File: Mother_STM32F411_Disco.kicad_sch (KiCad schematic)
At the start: 15 parts

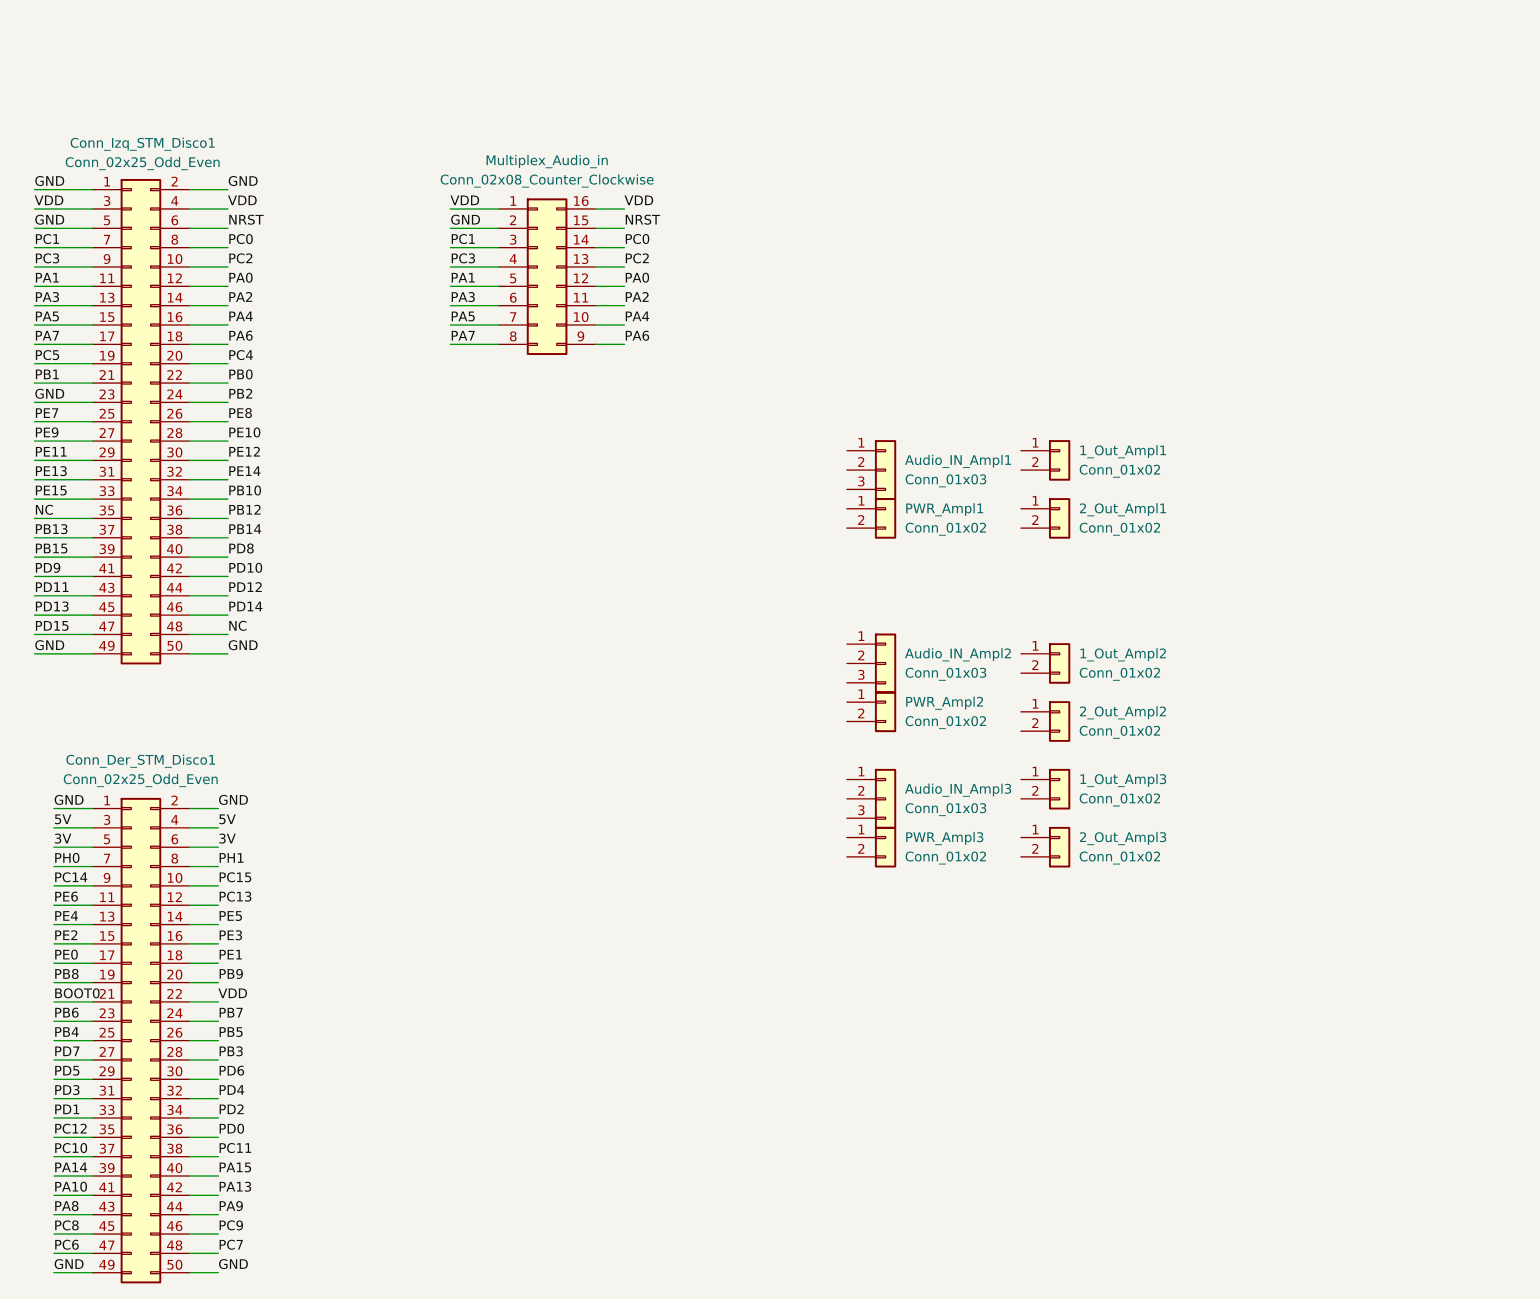
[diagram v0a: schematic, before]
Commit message: add modules in schematic
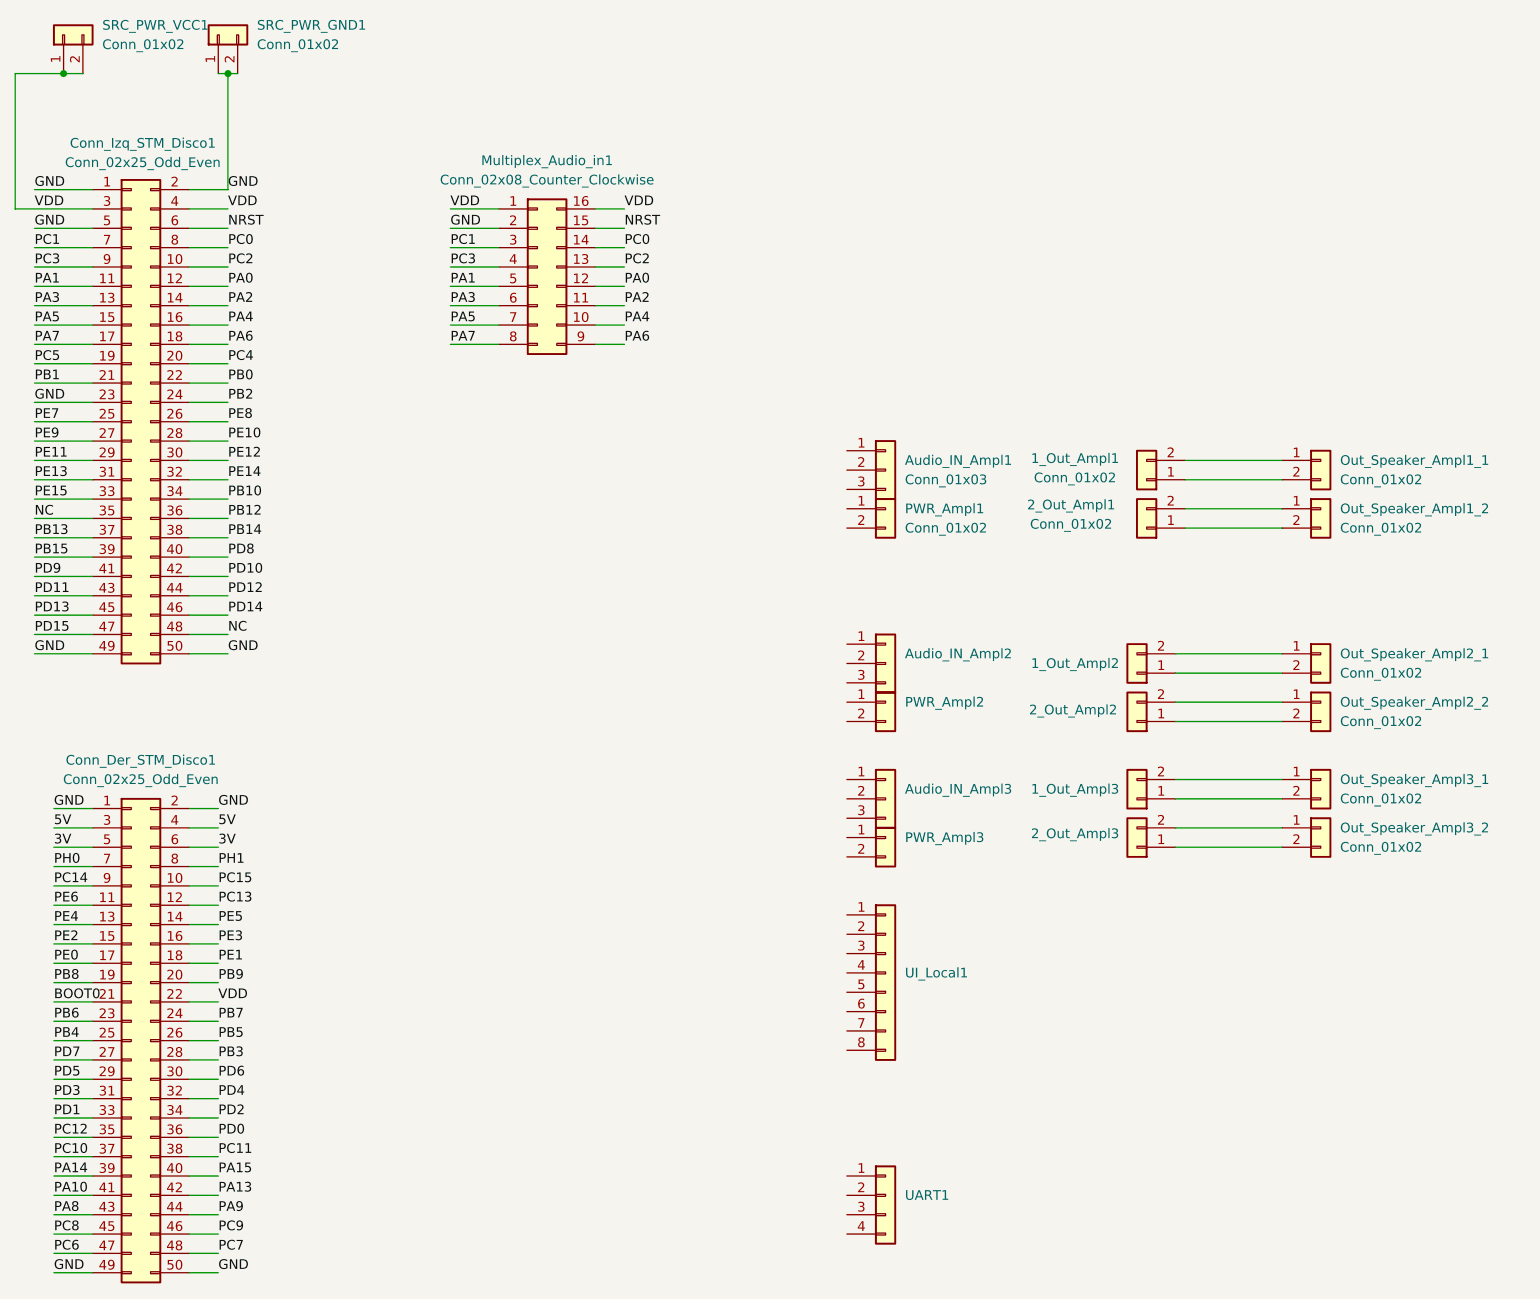
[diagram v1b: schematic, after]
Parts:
- added Out_Speaker_Ampl1_1, Out_Speaker_Ampl1_2, Out_Speaker_Ampl2_1, Out_Speaker_Ampl2_2, Out_Speaker_Ampl3_1, Out_Speaker_Ampl3_2: Conn_01x02, symbol Connector_Generic:Conn_01x02
- added SRC_PWR_GND1, SRC_PWR_VCC1: Conn_01x02, Connector_PinSocket_2.54mm:PinSocket_1x02_P2.54mm_Vertical, symbol Connector_Generic:Conn_01x02
- added UART1: Conn_01x04, symbol Connector_Generic:Conn_01x04
- added UI_Local1: Conn_01x08, symbol Connector_Generic:Conn_01x08
- renumbered Multiplex_Audio_in to Multiplex_Audio_in1
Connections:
- net GND: now also SRC_PWR_GND1.1 (Pin_1), SRC_PWR_GND1.2 (Pin_2)
- net VDD: now also SRC_PWR_VCC1.1 (Pin_1), SRC_PWR_VCC1.2 (Pin_2)
- net at 2_Out_Ampl2.1 (Pin_1): now also Out_Speaker_Ampl2_2.2 (Pin_2)
- net at 2_Out_Ampl2.2 (Pin_2): now also Out_Speaker_Ampl2_2.1 (Pin_1)
- net at 1_Out_Ampl2.1 (Pin_1): now also Out_Speaker_Ampl2_1.2 (Pin_2)
- net at 1_Out_Ampl2.2 (Pin_2): now also Out_Speaker_Ampl2_1.1 (Pin_1)
- net at 1_Out_Ampl1.1 (Pin_1): now also Out_Speaker_Ampl1_1.2 (Pin_2)
- net at 1_Out_Ampl1.2 (Pin_2): now also Out_Speaker_Ampl1_1.1 (Pin_1)
- net at 2_Out_Ampl1.1 (Pin_1): now also Out_Speaker_Ampl1_2.2 (Pin_2)
- net at 2_Out_Ampl1.2 (Pin_2): now also Out_Speaker_Ampl1_2.1 (Pin_1)
- net at 1_Out_Ampl3.1 (Pin_1): now also Out_Speaker_Ampl3_1.2 (Pin_2)
- net at 1_Out_Ampl3.2 (Pin_2): now also Out_Speaker_Ampl3_1.1 (Pin_1)
- net at 2_Out_Ampl3.1 (Pin_1): now also Out_Speaker_Ampl3_2.2 (Pin_2)
- net at 2_Out_Ampl3.2 (Pin_2): now also Out_Speaker_Ampl3_2.1 (Pin_1)
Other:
- moved on the sheet: 1_Out_Ampl1, 1_Out_Ampl2, 1_Out_Ampl3, 2_Out_Ampl1, 2_Out_Ampl2, 2_Out_Ampl3
